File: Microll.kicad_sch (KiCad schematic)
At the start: 36 parts, among them J1 Conn_01x12, J2 Conn_02x10_Top_Bottom, J3 Conn_01x08, J6 USB_C_Receptacle_USB2.0_16P, SW4 SW_DIP_x03, U1 ESP32-C3-WROOM-02-N4, U2 TLV76733DRVx, U3 STM32G0B1CBU6, U4 USBLC6-2P6, U5 DPDT_Switch_x2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

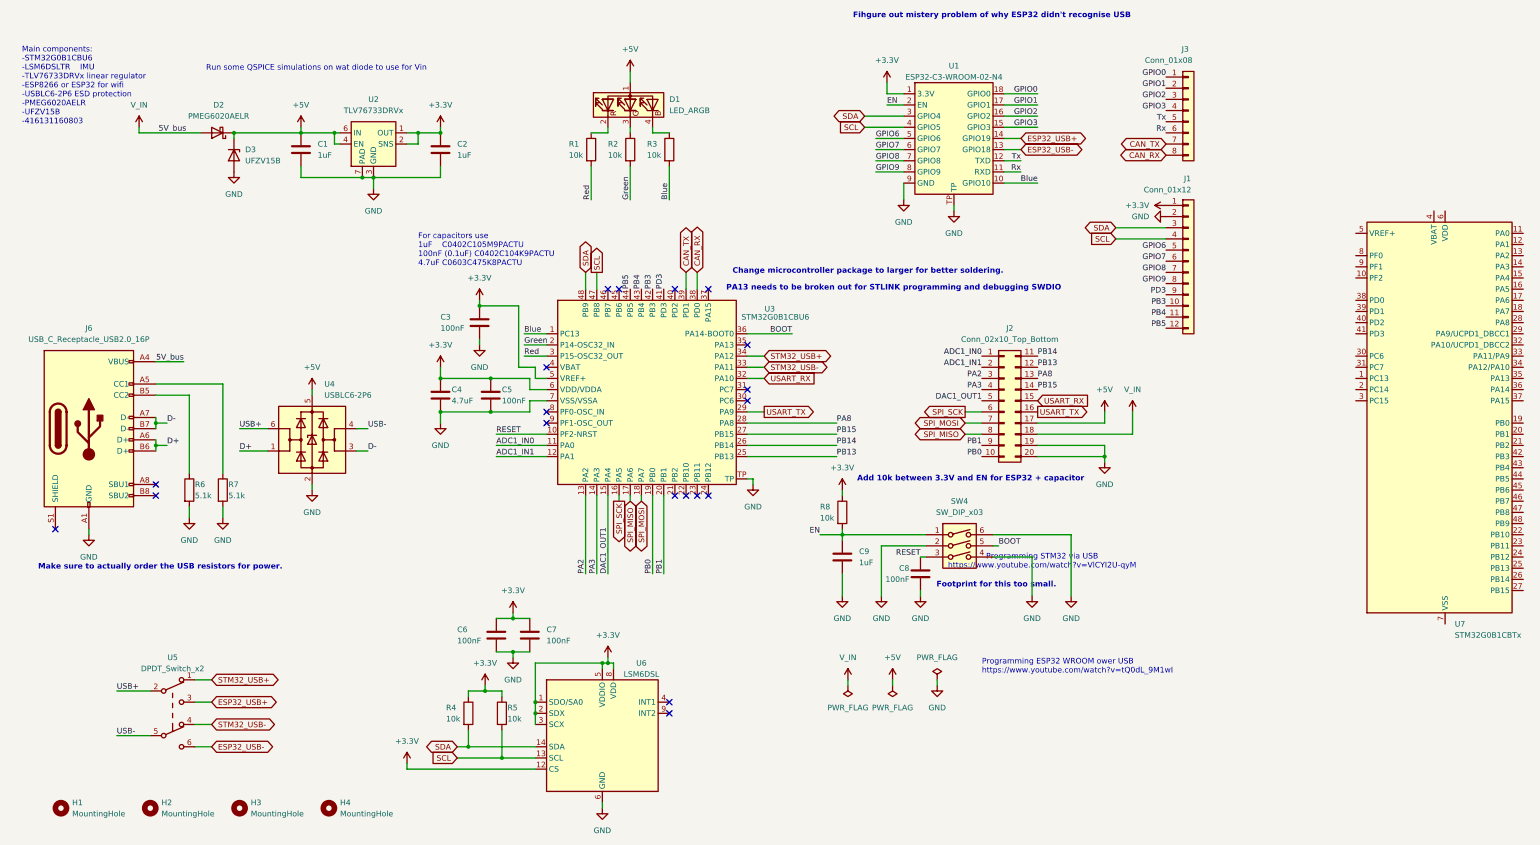
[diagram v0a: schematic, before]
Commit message: SWDIO and SWCLK now accessible through gpio pins. Microcontroller changed to more solder friendly package
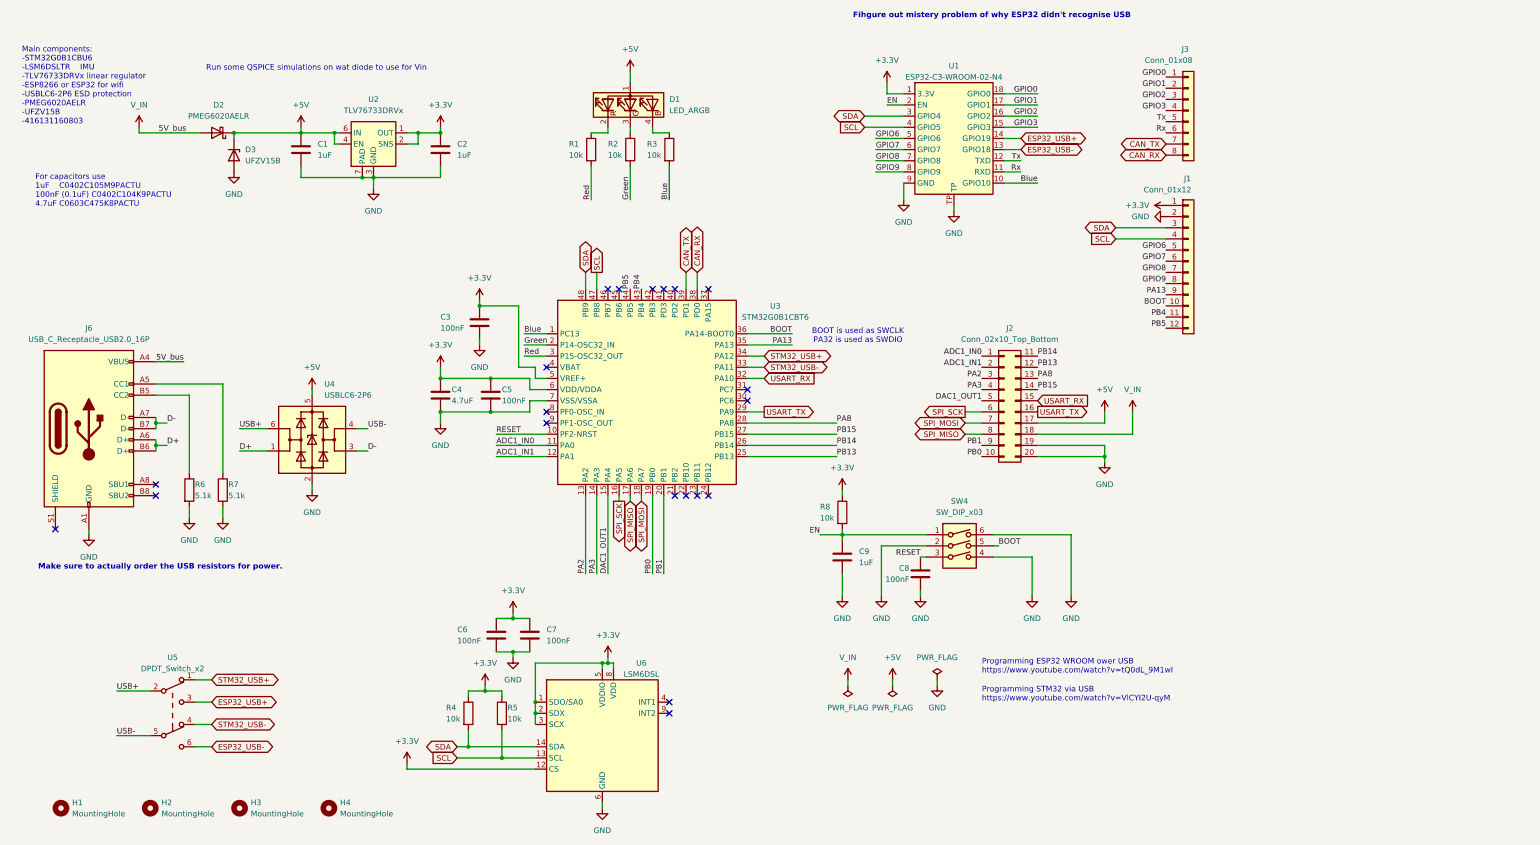
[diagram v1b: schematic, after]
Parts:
- removed U3: STM32G0B1CBU6, STM32:STM32G0B1CBU6, symbol STM32:STM32G0B1CBU6
- removed U7: STM32G0B1CBTx, Package_QFP:LQFP-48_7x7mm_P0.5mm, symbol MCU_ST_STM32G0:STM32G0B1CBTx
- added U3: STM32G0B1CBT6, Package_QFP:LQFP-48_7x7mm_P0.5mm, symbol STM32:STM32G0B1CBT6
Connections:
- net PB3 is gone; now on net BOOT: J1.10 (Pin_10)
- net +3.3V: now also U3.5 (VREF+), U3.6 (VDD/VDDA)
- net ADC1_IN0: now also U3.11 (PA0)
- net ADC1_IN1: now also U3.12 (PA1)
- net BOOT: now also U3.36 (PA14-BOOT0)
- net Blue: now also U3.1 (PC13)
- net CAN_RX: now also U3.38 (PD0)
- net CAN_TX: now also U3.39 (PD1)
- net DAC1_OUT1: now also U3.15 (PA4)
- net GND: now also U3.7 (VSS/VSSA)
- net Green: now also U3.2 (P14-OSC32_IN)
- net PA2: now also U3.13 (PA2)
- net PA3: now also U3.14 (PA3)
- net PA8: now also U3.28 (PA8)
- net PB0: now also U3.19 (PB0)
- net PB1: now also U3.20 (PB1)
- net PB13: now also U3.25 (PB13)
- net PB14: now also U3.26 (PB14)
- net PB15: now also U3.27 (PB15)
- net PB4: now also U3.43 (PB4)
- net PB5: now also U3.44 (PB5)
- net RESET: now also U3.10 (PF2-NRST)
- net Red: now also U3.3 (P15-OSC32_OUT)
- net SCL: now also U3.47 (PB8)
- net SDA: now also U3.48 (PB9)
- net SPI_MISO: now also U3.17 (PA6)
- net SPI_MOSI: now also U3.18 (PA7)
- net SPI_SCK: now also U3.16 (PA5)
- net STM32_USB+: now also U3.34 (PA12)
- net STM32_USB-: now also U3.33 (PA11)
- net USART_RX: now also U3.32 (PA10)
- net USART_TX: now also U3.29 (PA9)
- net PD3 renamed PA13
- net PA13: now also U3.35 (PA13)
- no-connect marks 19 -> 20
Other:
- note added: "BOOT is used as SWCLK PA32 is used as SWDIO"
- note removed: "Add 10k between 3.3V and EN for ESP32 + capacitor"
- note removed: "Change microcontroller package to larger for better soldering."
- note removed: "Footprint for this too small."
- note removed: "PA13 needs to be broken out for STLINK programming and debugging SWDIO"

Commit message: Made Microll V2 and updated Gerber Files
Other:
- note removed: "Fihgure out mistery problem of why ESP32 didn't recognise USB"
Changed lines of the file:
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@@
-		)
-	)
-	(text "Fihgure out mistery problem of why ESP32 didn't recognise USB"
-		(exclude_from_sim no)
-		(at 233.426 6.35 0)
-		(effects
-			(font
-				(size 1.27 1.27)
-				(bold yes)
-			)
 		)
 	)
@@
 			)
 		)
-		(property "Datasheet" ""
+		(property "Datasheet" "https://www.st.com/resource/en/datasheet/stm32g0b1cb.pdf"
 			(at 156.21 91.44 0)
 			(effects

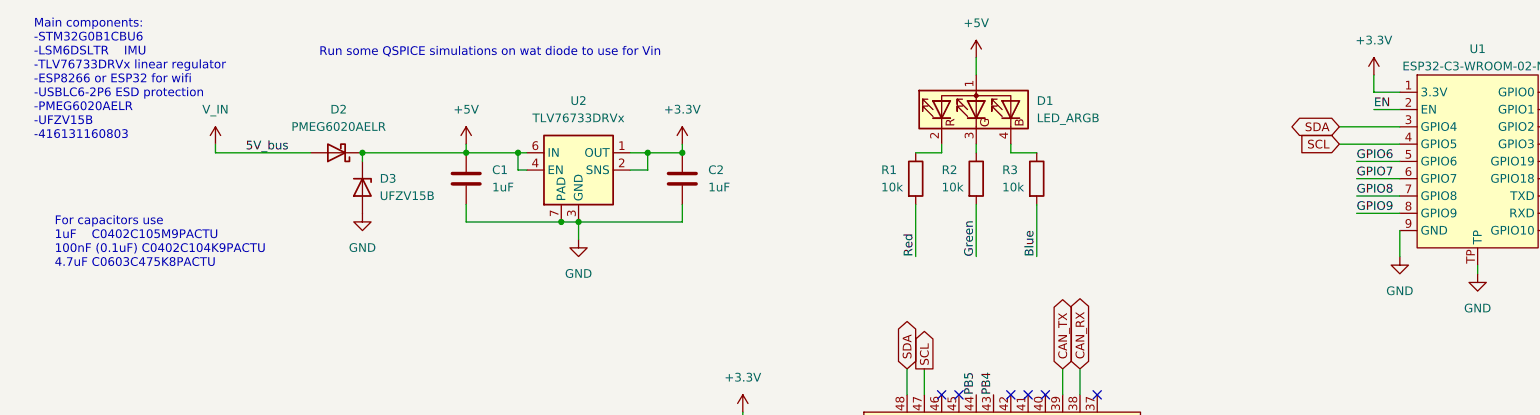
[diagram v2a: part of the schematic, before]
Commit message: Realized why I kept killing both the STM32 and ESP32. I stupidly connected the LEDs to 5V and was having the microcontrollers sink that. The micorcontroller pins can only handle 3.6V max. Even with the 10k current limiting resistors the voltage would damage them. Not to mention the 10k resistor is too little current to turn on thhe LEDs.
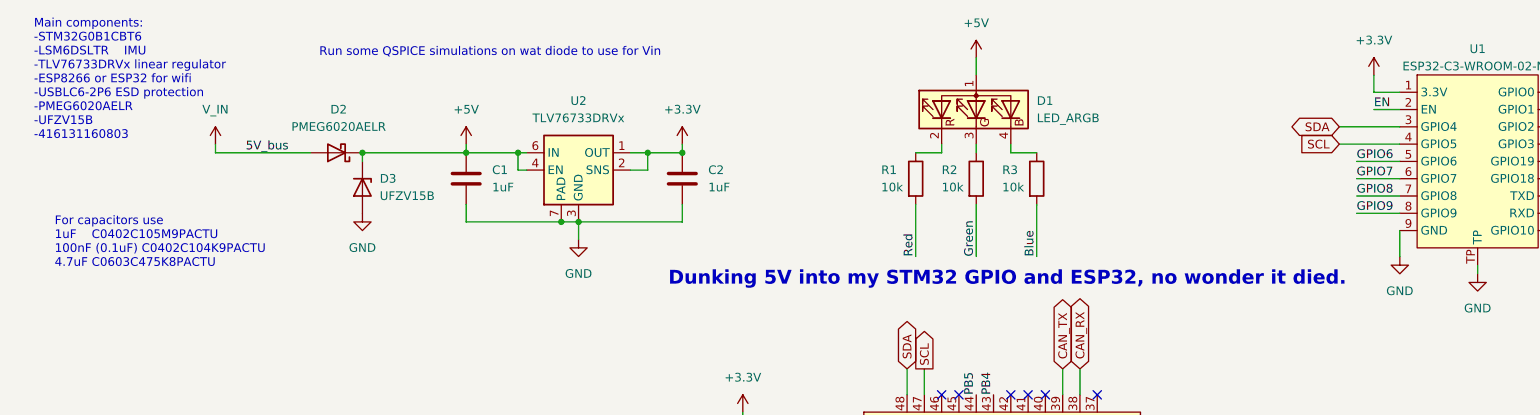
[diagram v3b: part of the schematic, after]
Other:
- note added: "Dunking 5V into my STM32 GPIO and ESP32, no wonder it died."
- note added: "Main components: -STM32G0B1CBT6 -LSM6DSLTR IMU -TLV76733DRVx linear regulator -ESP8266 or ESP32 for wifi -USBLC6-2P6 ESD protection -PMEG6020AELR -UFZV15B -416131160803"
- note removed: "Main components: -STM32G0B1CBU6 -LSM6DSLTR IMU -TLV76733DRVx linear regulator -ESP8266 or ESP32 for wifi -USBLC6-2P6 ESD protection -PMEG6020AELR -UFZV15B -416131160803"
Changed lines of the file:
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@@
+		)
+	)
+	(text "Dunking 5V into my STM32 GPIO and ESP32, no wonder it died."
+		(exclude_from_sim no)
+		(at 155.702 51.562 0)
+		(effects
+			(font
+				(size 2.032 2.032)
+				(thickness 0.508)
+				(bold yes)
+				(color 255 15 32 1)
+			)
 		)
 	)
@@
 		)
 	)
-	(text "Main components:\n-STM32G0B1CBU6	\n-LSM6DSLTR	IMU\n-TLV76733DRVx linear regulator\n-ESP8266 or ESP32 for wifi\n-USBLC6-2P6 ESD protection\n-PMEG6020AELR\n-UFZV15B\n-416131160803\n"
+	(text "Main components:\n-STM32G0B1CBT6	\n-LSM6DSLTR	IMU\n-TLV76733DRVx linear regulator\n-ESP8266 or ESP32 for wifi\n-USBLC6-2P6 ESD protection\n-PMEG6020AELR\n-UFZV15B\n-416131160803\n"
 		(exclude_from_sim no)
 		(at 12.7 31.242 0)

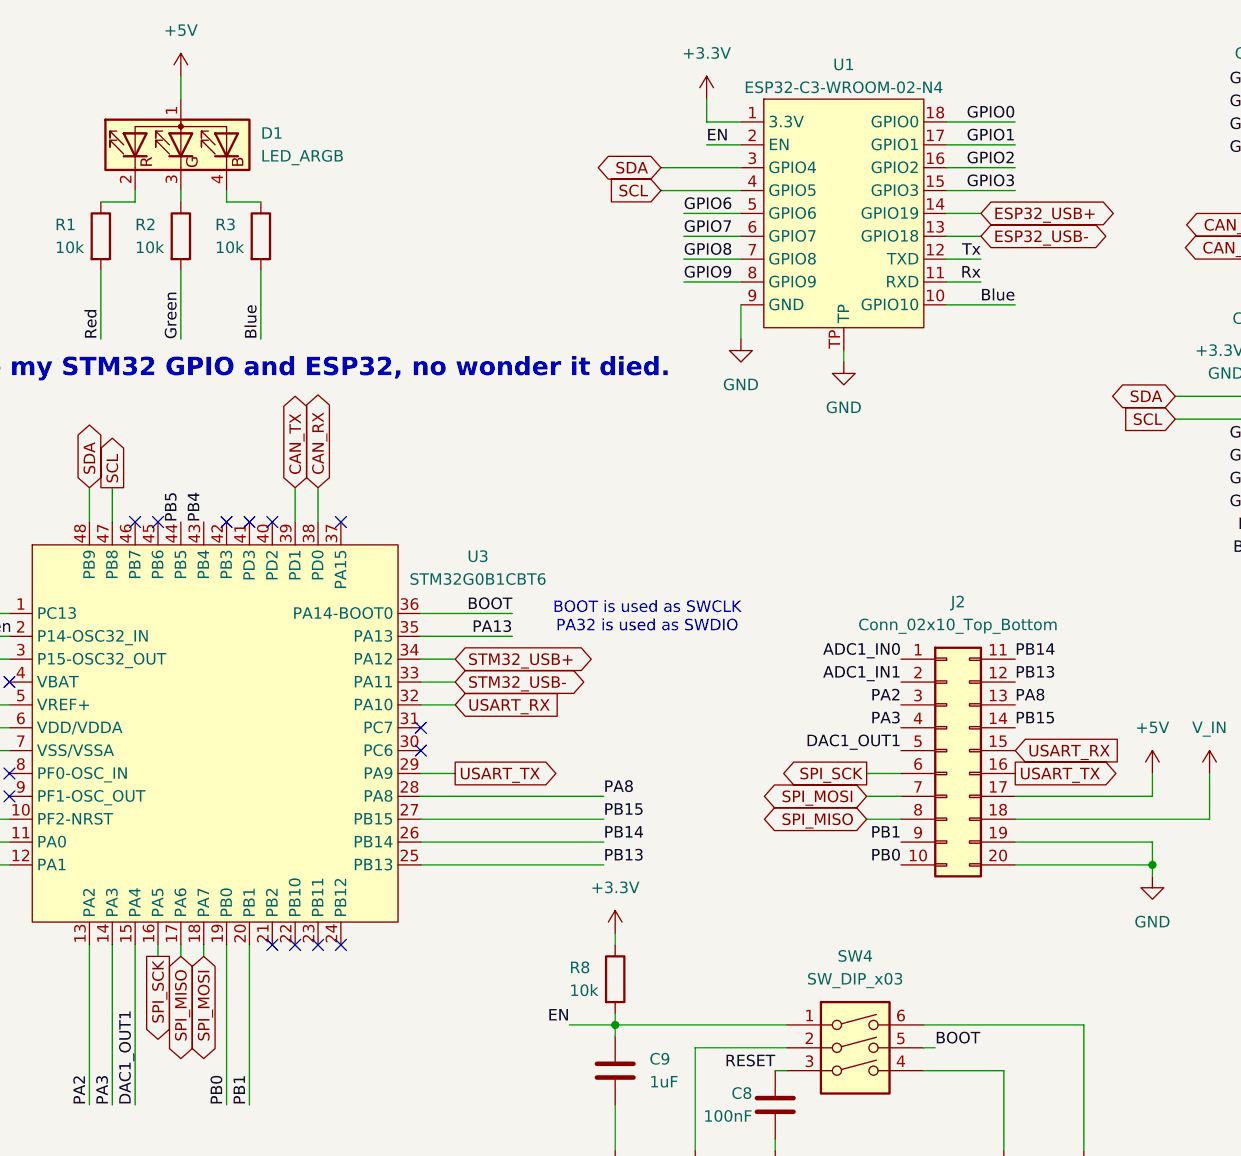
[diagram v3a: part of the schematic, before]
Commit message: small notes added on what will be changed. Schematic doc includes revision
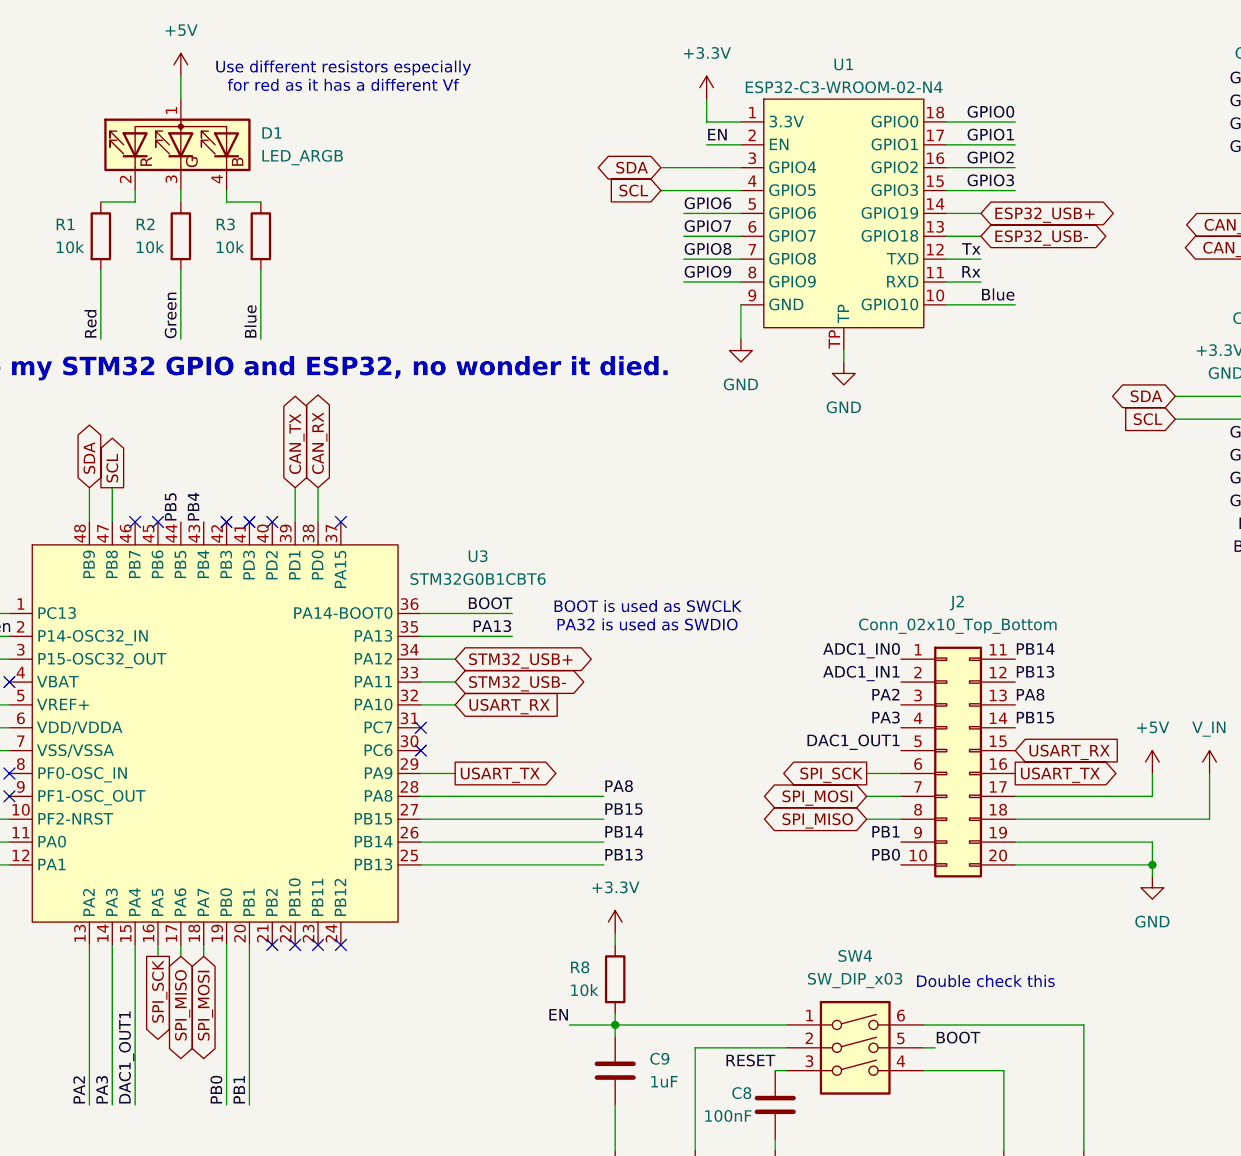
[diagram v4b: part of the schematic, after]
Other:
- note added: "Double check this"
- note added: "Use different resistors especially for red as it has a different Vf"
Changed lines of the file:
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@@
 	(title_block
 		(title "Microll")
+		(date "2024-09-03")
+		(rev "3")
 	)
 	(junction
@@
 		)
 	)
+	(text "Double check this"
+		(exclude_from_sim no)
+		(at 240.538 119.888 0)
+		(effects
+			(font
+				(size 1.27 1.27)
+			)
+		)
+	)
+	(text "Use different resistors especially\nfor red as it has a different Vf\n "
+		(exclude_from_sim no)
+		(at 169.164 20.32 0)
+		(effects
+			(font
+				(size 1.27 1.27)
+			)
+		)
+	)
